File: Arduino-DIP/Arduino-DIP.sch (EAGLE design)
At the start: 16 parts, among them IC1 ATMEGA 328, IC2 MCP1702-33, X1 16 MHz

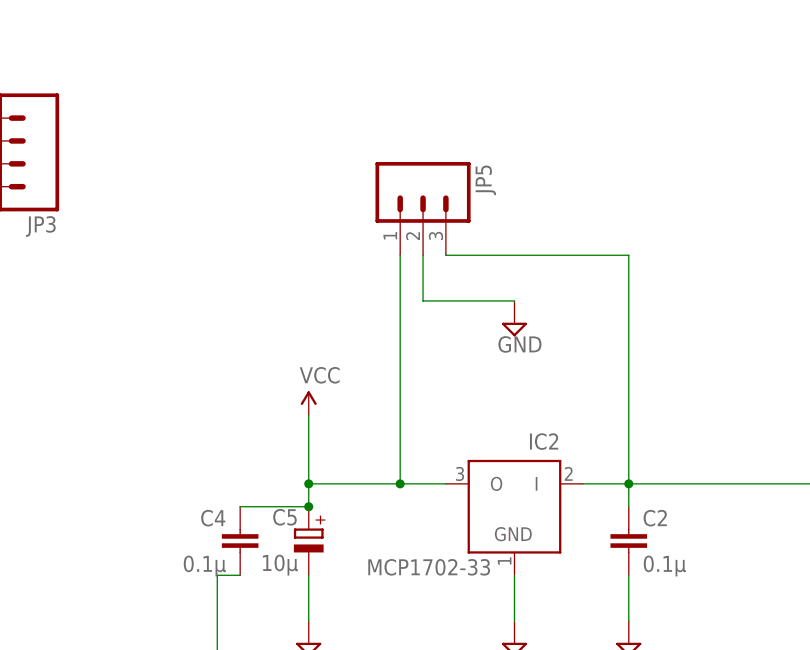
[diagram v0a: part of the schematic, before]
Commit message: finished routing DIP board and added tool patch for 1/32
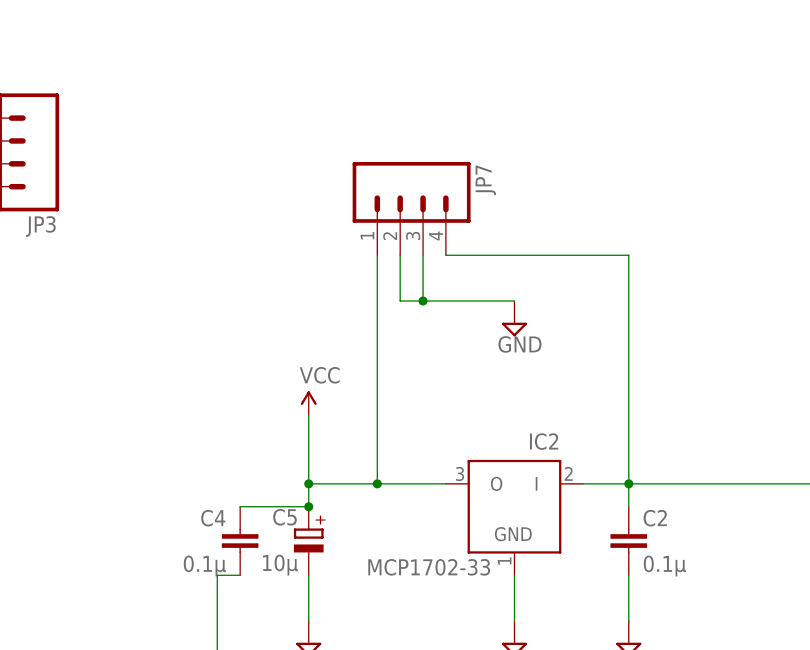
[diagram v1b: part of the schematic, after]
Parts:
- removed JP5: (no value), SparkFun-Connectors:M03PTH
- added JP7: (no value), SparkFun-Connectors:M04PTH
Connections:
- net GND: now also JP7.2, JP7.3; no longer JP5.2
- net PWR: now also JP7.4; no longer JP5.3
- net VCC: now also JP7.1; no longer JP5.1
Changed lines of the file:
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@@
 <part name="JP1" library="SparkFun-Connectors" deviceset="M05" device="PTH"/>
 <part name="JP3" library="SparkFun-Connectors" deviceset="M04" device="PTH"/>
-<part name="JP5" library="SparkFun-Connectors" deviceset="M03" device="PTH"/>
 <part name="R2" library="SparkFun-Passives" deviceset="RESISTOR" device="PTH-1/6W" value="10k"/>
 <part name="JP4" library="SparkFun-Connectors" deviceset="M01" device="PTH"/>
 <part name="C6" library="SparkFun-Capacitors" deviceset="CAP" device="PTH1" value="0.1uF"/>
+<part name="JP7" library="SparkFun-Connectors" deviceset="M04" device="PTH"/>
 </parts>
 <sheets>
@@
 <instance part="JP1" gate="G$1" x="144.78" y="86.36" rot="R180"/>
 <instance part="JP3" gate="G$1" x="154.94" y="101.6" rot="R180"/>
-<instance part="JP5" gate="G$1" x="200.66" y="96.52" rot="R270"/>
 <instance part="R2" gate="G$1" x="12.7" y="147.32" rot="R90"/>
 <instance part="JP4" gate="G$1" x="27.94" y="147.32" rot="R270"/>
 <instance part="C6" gate="G$1" x="53.34" y="40.64"/>
+<instance part="JP7" gate="G$1" x="198.12" y="93.98" rot="R270"/>
 </instances>
 <busses>
@@
 <wire x1="200.66" y1="83.82" x2="210.82" y2="83.82" width="0.1524" layer="91"/>
 <pinref part="SUPPLY1" gate="GND" pin="GND"/>
-<pinref part="JP5" gate="G$1" pin="2"/>
+<pinref part="JP7" gate="G$1" pin="3"/>
+<pinref part="JP7" gate="G$1" pin="2"/>
+<wire x1="200.66" y1="83.82" x2="198.12" y2="83.82" width="0.1524" layer="91"/>
+<wire x1="198.12" y1="83.82" x2="198.12" y2="88.9" width="0.1524" layer="91"/>
+<junction x="200.66" y="83.82"/>
 </segment>
 </net>
@@
 <segment>
 <pinref part="IC2" gate="G$1" pin="O"/>
-<wire x1="187.96" y1="63.5" x2="198.12" y2="63.5" width="0.1524" layer="91"/>
+<wire x1="187.96" y1="63.5" x2="195.58" y2="63.5" width="0.1524" layer="91"/>
 <pinref part="SUPPLY16" gate="1" pin="VCC"/>
-<wire x1="198.12" y1="63.5" x2="203.2" y2="63.5" width="0.1524" layer="91"/>
+<wire x1="195.58" y1="63.5" x2="203.2" y2="63.5" width="0.1524" layer="91"/>
 <wire x1="187.96" y1="71.12" x2="187.96" y2="63.5" width="0.1524" layer="91"/>
 <pinref part="C5" gate="G$1" pin="+"/>
@@
 <junction x="187.96" y="63.5"/>
 <junction x="187.96" y="60.96"/>
-<wire x1="198.12" y1="88.9" x2="198.12" y2="63.5" width="0.1524" layer="91"/>
-<junction x="198.12" y="63.5"/>
-<pinref part="JP5" gate="G$1" pin="1"/>
+<wire x1="195.58" y1="88.9" x2="195.58" y2="63.5" width="0.1524" layer="91"/>
+<junction x="195.58" y="63.5"/>
+<pinref part="JP7" gate="G$1" pin="1"/>
 </segment>
 <segment>
@@
 <pinref part="C2" gate="G$1" pin="1"/>
 <pinref part="FTDI" gate="1" pin="3"/>
-<pinref part="JP5" gate="G$1" pin="3"/>
 <wire x1="203.2" y1="88.9" x2="223.52" y2="88.9" width="0.1524" layer="91"/>
 <wire x1="223.52" y1="88.9" x2="223.52" y2="63.5" width="0.1524" layer="91"/>
-</segment>
-</net>
+<pinref part="JP7" gate="G$1" pin="4"/>
+</segment>
+</net>

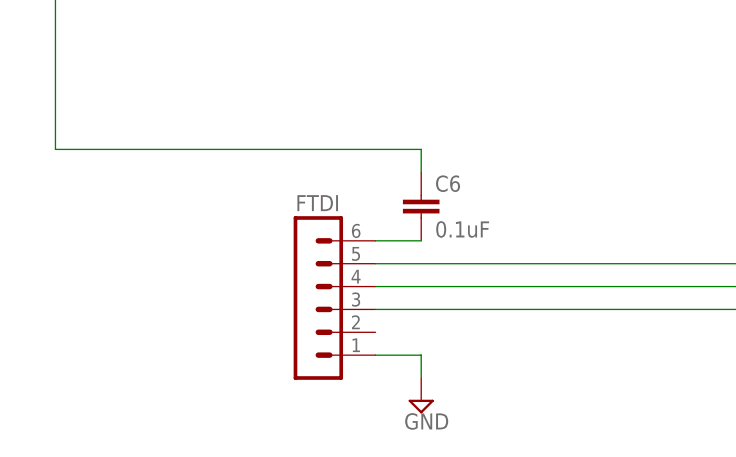
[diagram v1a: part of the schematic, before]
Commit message: added read me to SMD page
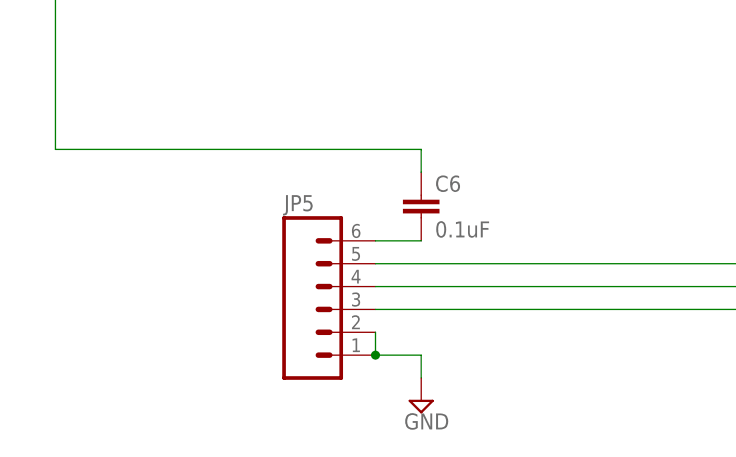
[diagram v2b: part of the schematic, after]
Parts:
- removed FTDI: FTDI, JeeLabs:MA06-1
- added JP5: (no value), SparkFun-Connectors:M06NO_SILK
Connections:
- net GND: now also JP5.1, JP5.2; no longer FTDI.1
- net N$20: now also JP5.6; no longer FTDI.6
- net PWR: now also JP5.3; no longer FTDI.3
- net RXD: now also JP5.4; no longer FTDI.4
- net TXD: now also JP5.5; no longer FTDI.5
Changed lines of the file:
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@@
 <part name="FRAME1" library="frames" deviceset="A4L-LOC" device="" value="protoype"/>
 <part name="IC1" library="atmega8" deviceset="ATMEGA48/88/168-PU" device="" value="ATMEGA 328"/>
-<part name="FTDI" library="JeeLabs" deviceset="MA06-1" device="" value="FTDI"/>
 <part name="SUPPLY4" library="SparkFun" deviceset="VCC" device=""/>
 <part name="SUPPLY6" library="SparkFun" deviceset="VCC" device=""/>
@@
 <part name="C6" library="SparkFun-Capacitors" deviceset="CAP" device="PTH1" value="0.1uF"/>
 <part name="JP7" library="SparkFun-Connectors" deviceset="M04" device="PTH"/>
+<part name="JP5" library="SparkFun-Connectors" deviceset="M06" device="NO_SILK"/>
 </parts>
 <sheets>
@@
 <instance part="FRAME1" gate="G$1" x="0" y="0"/>
 <instance part="IC1" gate="1" x="68.58" y="111.76"/>
-<instance part="FTDI" gate="1" x="40.64" y="33.02" smashed="yes">
-<attribute name="NAME" x="39.37" y="41.402" size="1.778" layer="95"/>
-</instance>
 <instance part="SUPPLY4" gate="1" x="12.7" y="154.94"/>
 <instance part="SUPPLY6" gate="1" x="33.02" y="114.3"/>
@@
 <instance part="C6" gate="G$1" x="53.34" y="40.64"/>
 <instance part="JP7" gate="G$1" x="198.12" y="93.98" rot="R270"/>
+<instance part="JP5" gate="G$1" x="43.18" y="30.48"/>
 </instances>
 <busses>
@@
 <wire x1="48.26" y1="25.4" x2="53.34" y2="25.4" width="0.1524" layer="91"/>
 <wire x1="53.34" y1="25.4" x2="53.34" y2="22.86" width="0.1524" layer="91"/>
-<pinref part="FTDI" gate="1" pin="1"/>
 <pinref part="SUPPLY9" gate="GND" pin="GND"/>
+<pinref part="JP5" gate="G$1" pin="1"/>
+<pinref part="JP5" gate="G$1" pin="2"/>
+<wire x1="48.26" y1="25.4" x2="48.26" y2="27.94" width="0.1524" layer="91"/>
+<junction x="48.26" y="25.4"/>
 </segment>
 <segment>
@@
 <wire x1="124.46" y1="116.84" x2="124.46" y2="33.02" width="0.1524" layer="91"/>
 <wire x1="124.46" y1="33.02" x2="48.26" y2="33.02" width="0.1524" layer="91"/>
-<pinref part="FTDI" gate="1" pin="4"/>
 <pinref part="IC1" gate="1" pin="PD0(RXD/PCINT16)"/>
 <wire x1="124.46" y1="116.84" x2="106.68" y2="116.84" width="0.1524" layer="91"/>
@@
 <wire x1="106.68" y1="116.84" x2="99.06" y2="116.84" width="0.1524" layer="91"/>
 <junction x="106.68" y="116.84"/>
+<pinref part="JP5" gate="G$1" pin="4"/>
 </segment>
 </net>
@@
 <wire x1="121.92" y1="35.56" x2="48.26" y2="35.56" width="0.1524" layer="91"/>
 <pinref part="IC1" gate="1" pin="PD1(TXD/PCINT17)"/>
-<pinref part="FTDI" gate="1" pin="5"/>
 <pinref part="JP2" gate="G$1" pin="2"/>
 <junction x="106.68" y="114.3"/>
+<pinref part="JP5" gate="G$1" pin="5"/>
 </segment>
 </net>
@@
 <segment>
 <wire x1="48.26" y1="38.1" x2="53.34" y2="38.1" width="0.1524" layer="91"/>
-<pinref part="FTDI" gate="1" pin="6"/>
 <pinref part="C6" gate="G$1" pin="2"/>
+<pinref part="JP5" gate="G$1" pin="6"/>
 </segment>
 </net>
@@
 <pinref part="IC2" gate="G$1" pin="I"/>
 <pinref part="C2" gate="G$1" pin="1"/>
-<pinref part="FTDI" gate="1" pin="3"/>
 <wire x1="203.2" y1="88.9" x2="223.52" y2="88.9" width="0.1524" layer="91"/>
 <wire x1="223.52" y1="88.9" x2="223.52" y2="63.5" width="0.1524" layer="91"/>
 <pinref part="JP7" gate="G$1" pin="4"/>
-</segment>
-</net>
+<pinref part="JP5" gate="G$1" pin="3"/>
+</segment>
+</net>
